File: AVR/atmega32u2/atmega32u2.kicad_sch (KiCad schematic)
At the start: 13 parts

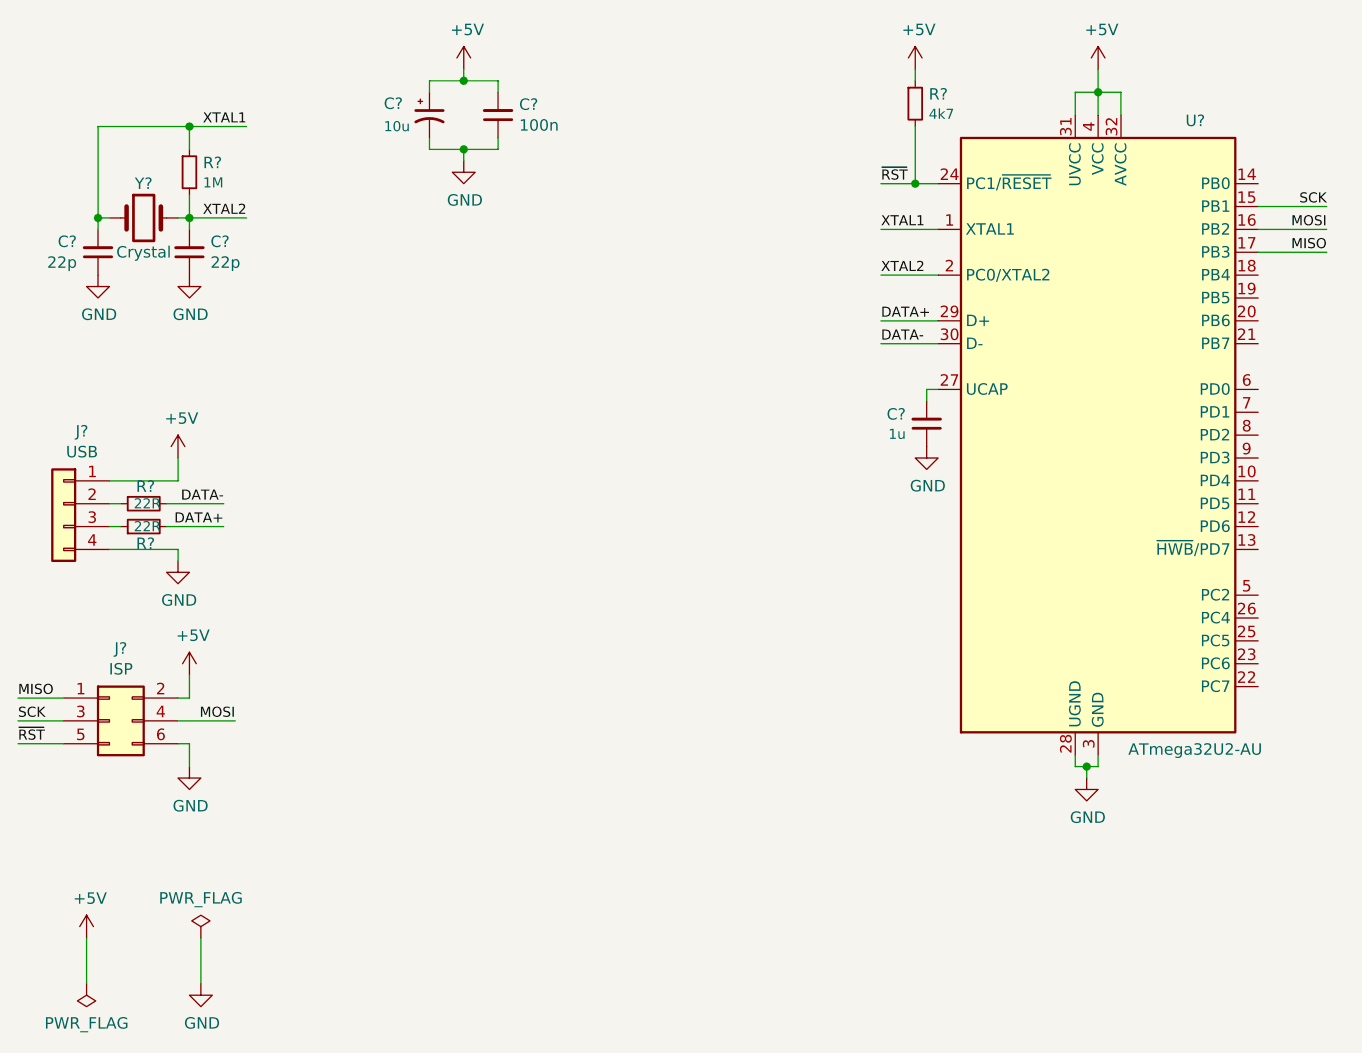
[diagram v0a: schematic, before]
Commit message: Fix grid alignment and update to KiCad 9
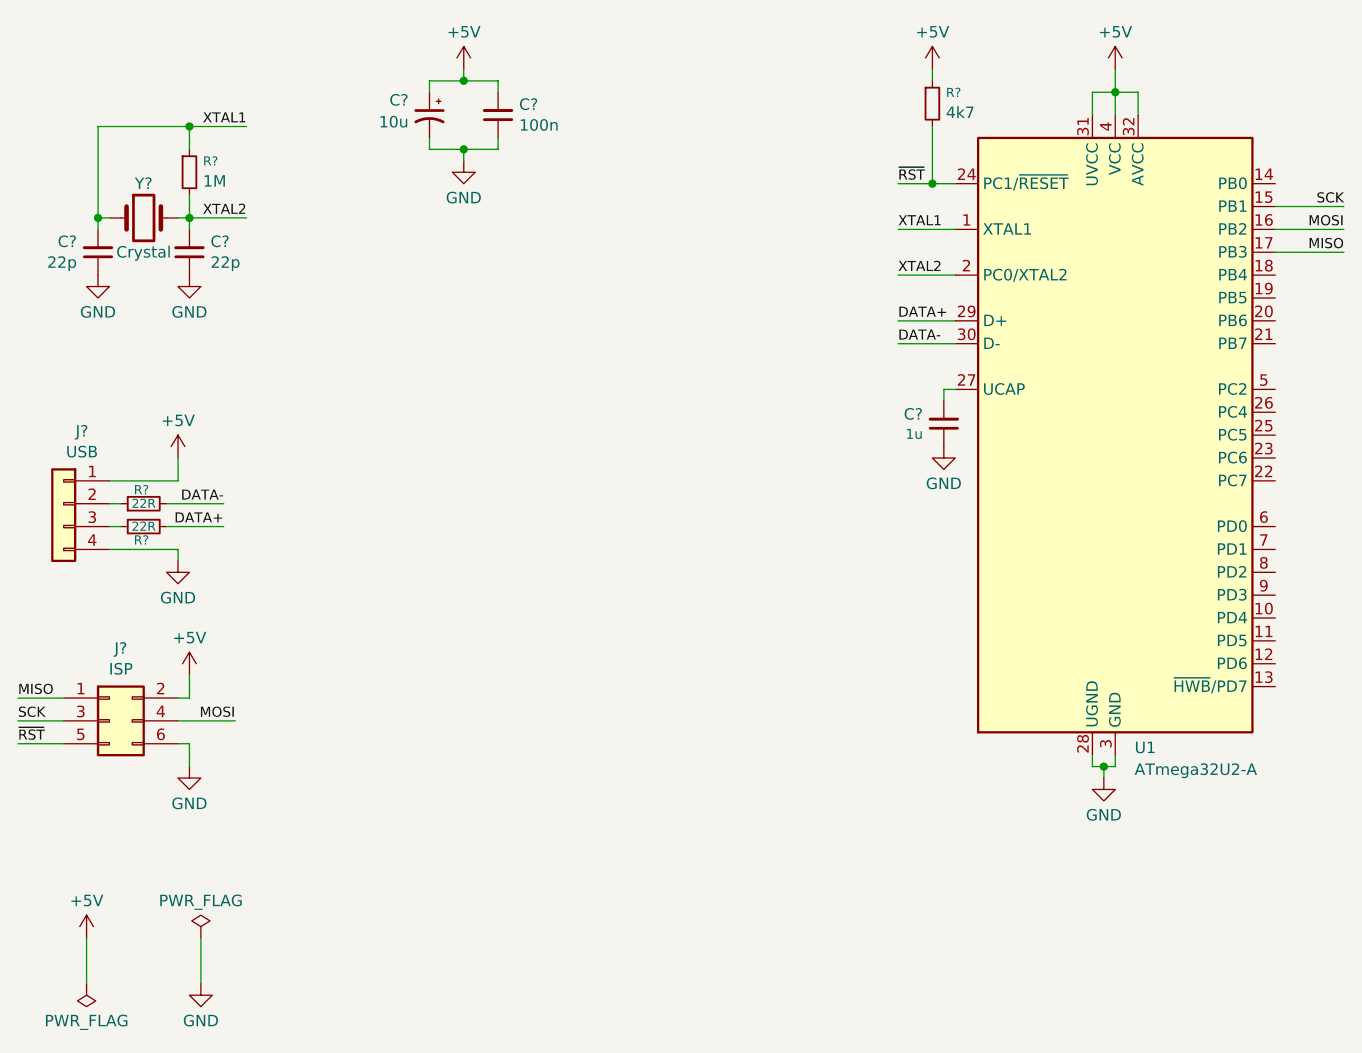
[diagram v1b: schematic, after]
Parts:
- removed C?: 10u, symbol Device:CP1_Small
- removed R?: 1M, symbol Device:R_Small
- removed R?: 4k7, symbol Device:R_Small
- removed R? (x2): 22R, symbol Device:R_Small
- removed U?: ATmega32U2-AU, Package_QFP:TQFP-32_7x7mm_P0.8mm, symbol atmega32u2-rescue:ATmega32U2-AU-MCU_Microchip_ATmega
- added C?: 10u, symbol Device:C_Polarized_Small_US
- added R?: 1M, symbol Device:R_Small
- added R? (x2): 22R, symbol Device:R_Small
- added R?: 4k7, symbol Device:R_Small
- added U1: ATmega32U2-A, Package_QFP:TQFP-32_7x7mm_P0.8mm, symbol MCU_Microchip_ATmega:ATmega32U2-A
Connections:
- net +5V: now also C?.1, R?.1, U1.31 (UVCC), U1.32 (AVCC), U1.4 (VCC)
- net DATA+: now also R?.2, U1.29 (D+)
- net DATA-: now also R?.2, U1.30 (D-)
- net GND: now also C?.2, U1.28 (UGND), U1.3 (GND)
- net MISO: now also U1.17 (PB3)
- net MOSI: now also U1.16 (PB2)
- net SCK: now also U1.15 (PB1)
- net XTAL1: now also R?.1, U1.1 (XTAL1)
- net XTAL2: now also R?.2, U1.2 (PC0/XTAL2)
- net ~{RST}: now also R?.2, U1.24 (PC1/~{RESET})
- net at C?.2: now also U1.27 (UCAP)
- net at J?.2 (Pin_2): now also R?.1
- net at J?.3 (Pin_3): now also R?.1
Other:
- moved on the sheet: C?
